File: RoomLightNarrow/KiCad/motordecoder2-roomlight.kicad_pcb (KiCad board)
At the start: 2 copper layers, 87 x 10 mm, 87 parts, among them J11 PAD, J12 PAD, J13 PAD, J14 PAD, J15 PAD, J16 PAD, J17 PAD, J18 PAD, J19 PAD, J21 PAD, J22 PAD, P1 PAD, P10 PAD, P11 PAD, P3 PAD, P5 PAD, P6 PAD, P7 PAD, P8 PAD, P9 PROG, Q1 DMG6601LVT, Q11 SSM3K7002BFU, Q12 SSM3K7002BFU, Q13 SSM6N7002BFE, Q14 SSM6N7002BFE, Q17 SSM3K7002BFU, Q2 DMG6601LVT, Q21 PMBT3906VS, Q22 SSM6N7002BFE, Q3 PMBT3904VS, Q5 2SC4116, Q6 PMBT3906VS, Q8 PMBT3904VS, U2 ATtiny1606-M

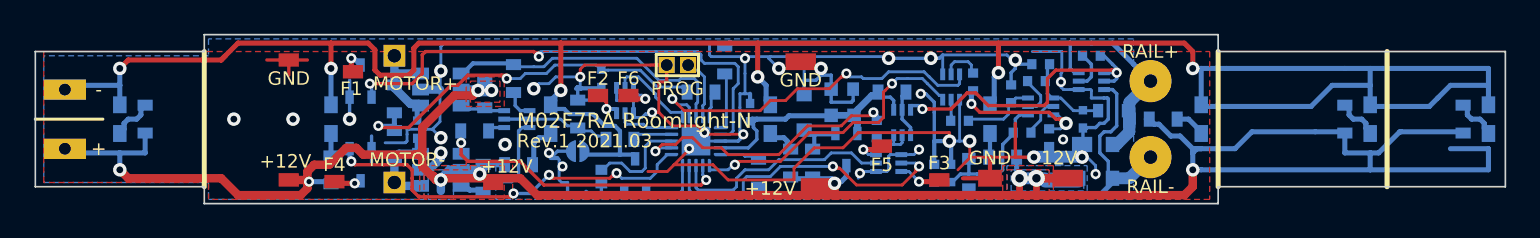
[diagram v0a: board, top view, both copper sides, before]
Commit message: 回路の問題点を修正 (K3066: Rev3 / それ以外: Rev2)
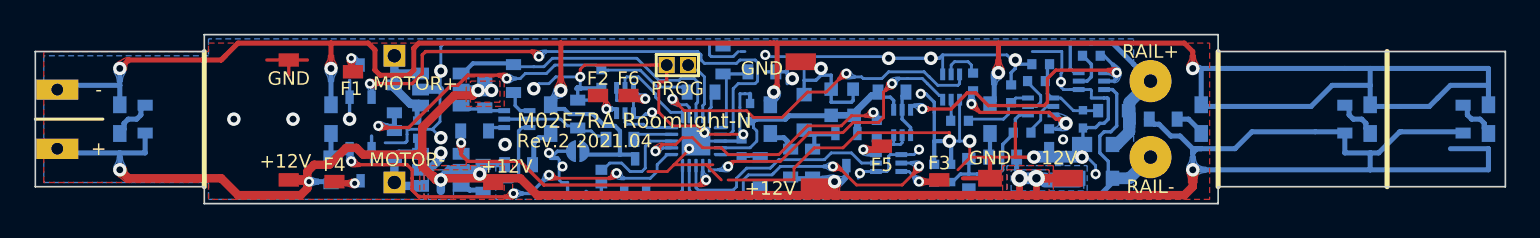
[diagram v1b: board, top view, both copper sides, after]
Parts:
- removed C6: 104, footprint:C_1005_v2
- added R16: 103, footprint:R_1005, B.Cu at (190.5, 107.6)
- added R17: 104, footprint:R_1608_v2, B.Cu at (200.0, 107.2)
- added R18: 104, footprint:R_1005, B.Cu at (198.8, 111.7)
- C7: value 104 -> 182
- moved J21 0.45 mm to (158.3, 111.8)
- moved J22 0.45 mm to (158.3, 108.2)
- moved R2 0.14 mm to (199.9, 113.1)
- moved R1 0.10 mm to (197.7, 106.5)
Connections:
- Q12 pad 1: Func2 -> Func4
- Q13 pad 2: Func3 -> Func5
- Q13 pad 5: Func4 -> Func3
- Q14 pad 2: Func5 -> Func6
- Q14 pad 5: Func6 -> Func2
- U2 pad 11: Func2 -> Func4
- U2 pad 15: Func5 -> Func6
- U2 pad 16: Func6 -> Func2
- U2 pad 8: Func4 -> Func3
- U2 pad 9: Func3 -> Func5
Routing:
- net Func2: track 23.7 -> 5.23 mm, vias 4 -> 0
- net Func5: track 3.42 -> 19.2 mm, vias 0 -> 2
- net Func4: track 13.6 -> 23.7 mm, vias 0 -> 4
- net Func3: track 19.2 -> 13.6 mm, vias 2 -> 0
- net GND: track 180.0 -> 175.8 mm
- net Func1: track 30.0 -> 32.3 mm
- net Func6: track 5.23 -> 3.42 mm
- net Net-(R1-Pad2): track 3.62 -> 5.14 mm
- net Net-(D41-Pad1): track 143.0 -> 144.0 mm
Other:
- board text added: "Rev.2 2021.04"
- board text removed: "Rev.1 2021.03"

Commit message: 基板上のF表記をP表記に変更
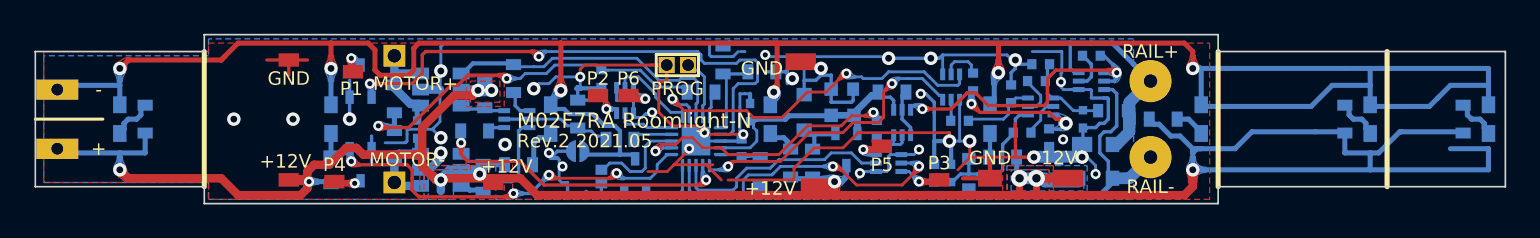
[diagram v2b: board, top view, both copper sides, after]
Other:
- board text added: "P1"
- board text added: "P2"
- board text added: "P3"
- board text added: "P4"
- board text added: "P5"
- board text added: "P6"
- board text added: "P7"
- board text added: "Rev.2 2021.05"
- board text removed: "F1"
- board text removed: "F2"
- board text removed: "F3"
- board text removed: "F4"
- board text removed: "F5"
- board text removed: "F6"
- board text removed: "F7"
- board text removed: "Rev.2 2021.04"
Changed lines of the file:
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@@
     (effects (font (size 0.8 0.8) (thickness 0.2)))
   )
-  (gr_text F1 (at 175.7 108.2) (layer F.SilkS)
+  (gr_text P1 (at 175.7 108.2) (layer F.SilkS)
     (effects (font (size 0.8 0.8) (thickness 0.17)))
   )
-  (gr_text F4 (at 174.7 112.7) (layer F.SilkS)
+  (gr_text P4 (at 174.7 112.7) (layer F.SilkS)
     (effects (font (size 0.8 0.8) (thickness 0.17)))
   )
-  (gr_text F7 (at 187.75 112 270) (layer B.SilkS)
+  (gr_text P7 (at 187.75 112 270) (layer B.SilkS)
     (effects (font (size 0.8 0.8) (thickness 0.2)) (justify mirror))
   )
@@
   )
   (gr_circle (center 198.3 109.7) (end 198.6 109.7) (layer B.SilkS) (width 0.15))
-  (gr_text F2 (at 190.3 107.6) (layer F.SilkS)
+  (gr_text P2 (at 190.3 107.6) (layer F.SilkS)
     (effects (font (size 0.8 0.8) (thickness 0.17)))
   )
-  (gr_text F3 (at 210.5 112.6) (layer F.SilkS)
+  (gr_text P3 (at 210.5 112.6) (layer F.SilkS)
     (effects (font (size 0.8 0.8) (thickness 0.17)))
   )
-  (gr_text F5 (at 207.1 112.7) (layer F.SilkS)
+  (gr_text P5 (at 207.1 112.7) (layer F.SilkS)
     (effects (font (size 0.8 0.8) (thickness 0.17)))
   )
-  (gr_text F6 (at 192.1 107.6) (layer F.SilkS)
+  (gr_text P6 (at 192.1 107.6) (layer F.SilkS)
     (effects (font (size 0.8 0.8) (thickness 0.17)))
   )
@@
   (gr_line (start 209.3 108.1) (end 61.55 108.1) (layer Dwgs.User) (width 0.15))
   (gr_line (start 245.25 109.25) (end 97.5 109.25) (layer Dwgs.User) (width 0.15))
-  (gr_text "Rev.2 2021.04" (at 185.5 111.3) (layer F.SilkS)
+  (gr_text "Rev.2 2021.05" (at 185.5 111.3) (layer F.SilkS)
     (effects (font (size 0.8 0.8) (thickness 0.18)) (justify left))
   )
